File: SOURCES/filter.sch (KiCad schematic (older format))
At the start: 52 parts, among them J1 RCA_01, J2 RCA_01, P8 CONN_02X03, P9 CONN_02X03, U3 LME49721, U4 LME49721

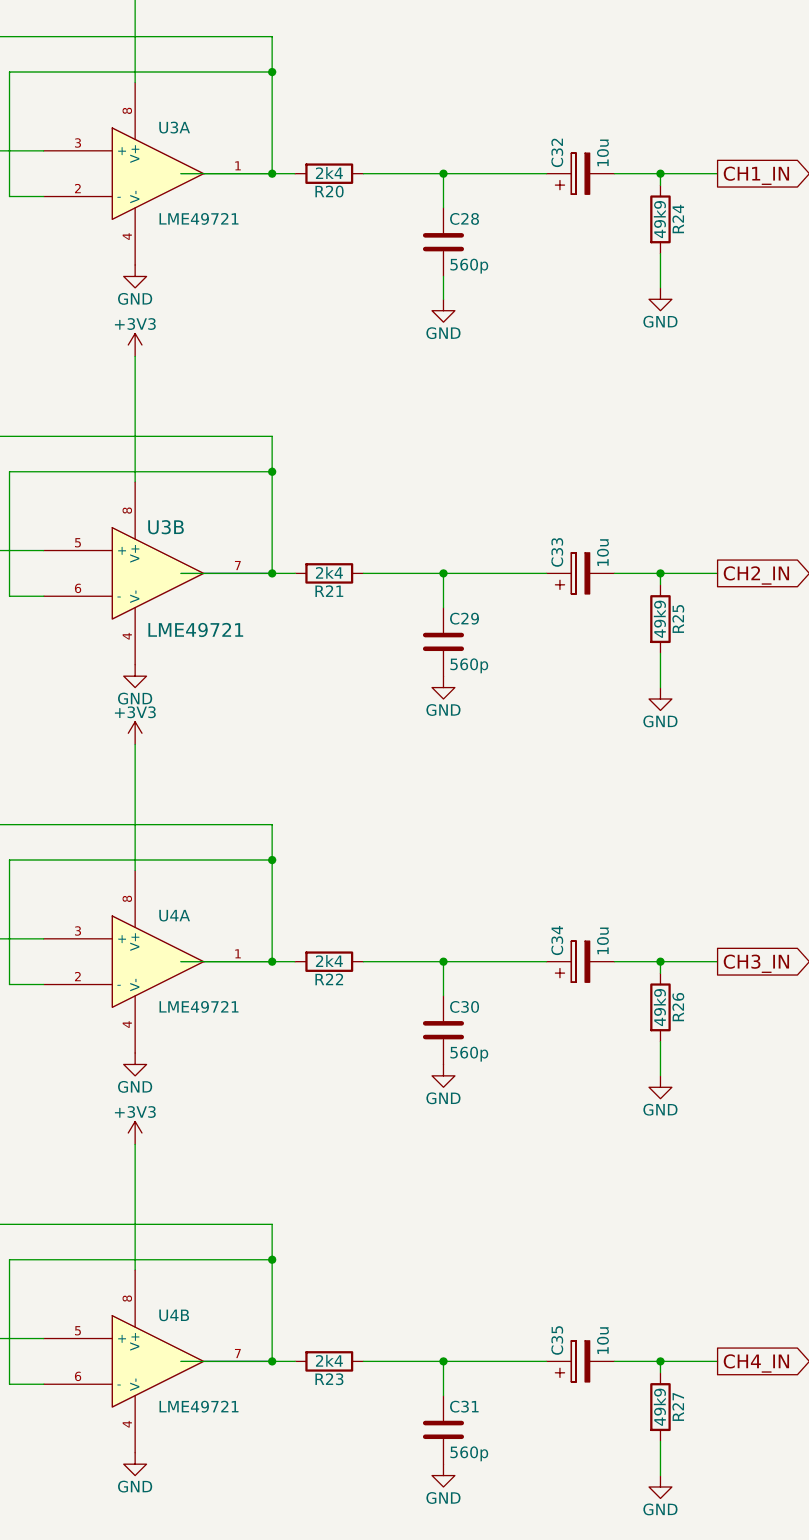
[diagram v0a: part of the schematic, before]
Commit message: changed filter resistors, clock resistors
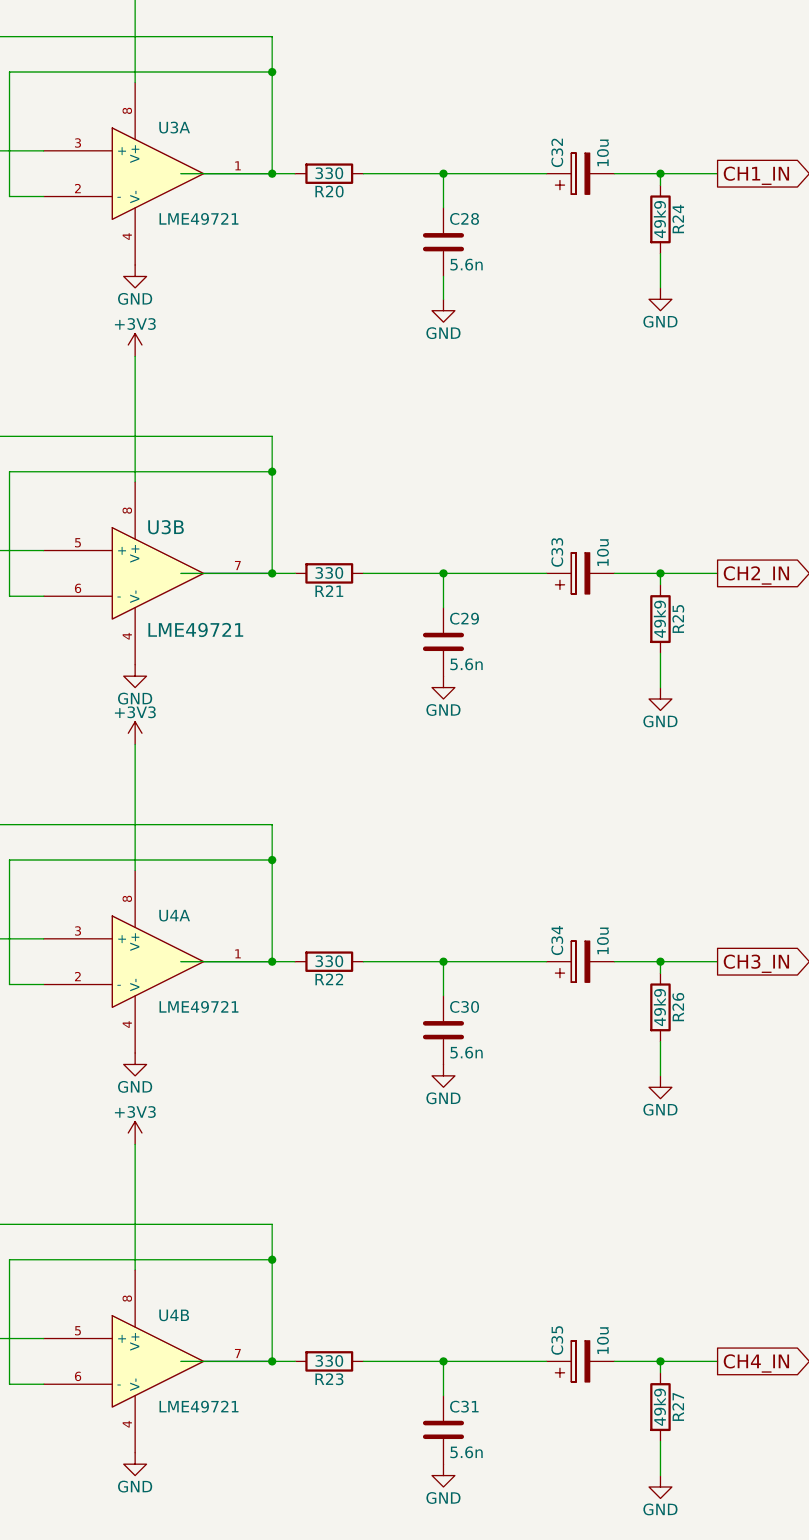
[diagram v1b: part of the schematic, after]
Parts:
- C28, C29, C30, C31: value 560p -> 5.6n
- R20, R21, R22, R23: value 2k4 -> 330
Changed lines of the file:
@@
 P 5200 2100
 F 0 "C28" H 5225 2200 50  0000 L CNN
-F 1 "560p" H 5225 2000 50  0000 L CNN
+F 1 "5.6n" H 5225 2000 50  0000 L CNN
 F 2 "fdsp_capacitor:C_1206_HandSoldering" H 5238 1950 50  0001 C CNN
 F 3 "" H 5200 2100 50  0000 C CNN
@@
 P 4700 1800
 F 0 "R20" V 4780 1800 50  0000 C CNN
-F 1 "2k4" V 4700 1800 50  0000 C CNN
+F 1 "330" V 4700 1800 50  0000 C CNN
 F 2 "fdsp_resistor:R_1206_HandSoldering" V 4630 1800 50  0001 C CNN
 F 3 "" H 4700 1800 50  0000 C CNN
@@
 P 5200 3850
 F 0 "C29" H 5225 3950 50  0000 L CNN
-F 1 "560p" H 5225 3750 50  0000 L CNN
+F 1 "5.6n" H 5225 3750 50  0000 L CNN
 F 2 "fdsp_capacitor:C_1206_HandSoldering" H 5238 3700 50  0001 C CNN
 F 3 "" H 5200 3850 50  0000 C CNN
@@
 P 4700 3550
 F 0 "R21" V 4780 3550 50  0000 C CNN
-F 1 "2k4" V 4700 3550 50  0000 C CNN
+F 1 "330" V 4700 3550 50  0000 C CNN
 F 2 "fdsp_resistor:R_1206_HandSoldering" V 4630 3550 50  0001 C CNN
 F 3 "" H 4700 3550 50  0000 C CNN
@@
 P 5200 5550
 F 0 "C30" H 5225 5650 50  0000 L CNN
-F 1 "560p" H 5225 5450 50  0000 L CNN
+F 1 "5.6n" H 5225 5450 50  0000 L CNN
 F 2 "fdsp_capacitor:C_1206_HandSoldering" H 5238 5400 50  0001 C CNN
 F 3 "" H 5200 5550 50  0000 C CNN
@@
 P 4700 5250
 F 0 "R22" V 4780 5250 50  0000 C CNN
-F 1 "2k4" V 4700 5250 50  0000 C CNN
+F 1 "330" V 4700 5250 50  0000 C CNN
 F 2 "fdsp_resistor:R_1206_HandSoldering" V 4630 5250 50  0001 C CNN
 F 3 "" H 4700 5250 50  0000 C CNN
@@
 P 5200 7300
 F 0 "C31" H 5225 7400 50  0000 L CNN
-F 1 "560p" H 5225 7200 50  0000 L CNN
+F 1 "5.6n" H 5225 7200 50  0000 L CNN
 F 2 "fdsp_capacitor:C_1206_HandSoldering" H 5238 7150 50  0001 C CNN
 F 3 "" H 5200 7300 50  0000 C CNN
@@
 P 4700 7000
 F 0 "R23" V 4780 7000 50  0000 C CNN
-F 1 "2k4" V 4700 7000 50  0000 C CNN
+F 1 "330" V 4700 7000 50  0000 C CNN
 F 2 "fdsp_resistor:R_1206_HandSoldering" V 4630 7000 50  0001 C CNN
 F 3 "" H 4700 7000 50  0000 C CNN
